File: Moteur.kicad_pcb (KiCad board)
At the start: 2 copper layers, 0 parts

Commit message: Couche PCB Définie
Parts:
- added C10: 10n, _0603, F.Cu at (76.2, 72.4)
- added C11, C12: 10pF, _0603, F.Cu at (0.00, 0.00)
- added C13, C6, C7, C9: 100n, _0603, F.Cu at (0.00, 0.00)
- added C14, C16: 47nF, SM1206, F.Cu at (0.00, 0.00)
- added C15: 47nF, SM1206, F.Cu at (48.3, 69.8)
- added R11: 100k, SM0805, F.Cu at (59.7, 52.1)
- added R8: 100k, SM0805, F.Cu at (34.3, 29.2)
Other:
- copper layers 2 -> 4
- net class Default: clearance 0.254 -> 0.204; trace_width 0.254 -> 0.204; via_dia 0.889 -> 0.8; via_drill 0.635 -> 0.3
- rule trace_clearance: 0.254 -> 0.204
- rule trace_min: 0.254 -> 0.204
- rule via_min_drill: 0.508 -> 0.3
- rule via_min_size: 0.889 -> 0.8

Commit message: footprints
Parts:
- added C1, C5: 100n, _0603, F.Cu at (0.00, 0.00)
- added C17, C8: 1uF, _0603, F.Cu at (0.00, 0.00)
- added C18: C, _0603, F.Cu at (0.00, 0.00)
- added C2: 100nF, _0603, F.Cu at (0.00, 0.00)
- added C3: 4.7uF, _0603, F.Cu at (0.00, 0.00)
- added C4: 470n, _0603, F.Cu at (0.00, 0.00)
- added D1: DIODESCH, CVRA-SOD80C, F.Cu at (0.00, 0.00)
- added D2: DEL_RGB, LedRGB, F.Cu at (0.00, 0.00)
- added IC1: TPS71501, CVRA-SOT23-5, F.Cu at (0.00, 0.00)
- added IC3: MAX3051, _SOT23-8, F.Cu at (0.00, 0.00)
- added JP1: JUMPER, Jumer, F.Cu at (0.00, 0.00)
- added L1: INDUCTOR, _0603, F.Cu at (0.00, 0.00)
- added P1: Bus2, _Pin2mm_4z, F.Cu at (0.00, 0.00)
- added P2: MotorEnc, _Pin2mm_5z, F.Cu at (0.00, 0.00)
- added P3: Bus1, _Pin2mm_4z, F.Cu at (0.00, 0.00)
- added P4: Motor, _Pin2mm_2, F.Cu at (0.00, 0.00)
- added P5: DBG, _Pin2mm_7z, F.Cu at (0.00, 0.00)
- added P6: PWR, _Pin2mm_2, F.Cu at (0.00, 0.00)
- added P7: GPIO, _Pin2mm_5z, F.Cu at (0.00, 0.00)
- added R1: 5.6M, _0603, F.Cu at (0.00, 0.00)
- added R10: 0.01R, CVRA-1206-1, F.Cu at (0.00, 0.00)
- added R12, R13: R, _0603, F.Cu at (0.00, 0.00)
- added R2: 910k, _0603, F.Cu at (0.00, 0.00)
- added R3: 0R, _0603, F.Cu at (0.00, 0.00)
- added R4: 22, _0603, F.Cu at (0.00, 0.00)
- added R5: 47, _0603, F.Cu at (0.00, 0.00)
- added R6: 39, _0603, F.Cu at (0.00, 0.00)
- added R7: 120, _0603, F.Cu at (0.00, 0.00)
- added R9: 330, _0603, F.Cu at (0.00, 0.00)
- added U1: STM32F303CCT6, _LQFP48, F.Cu at (0.00, 0.00)
- added X1: 16MHz, _TSX-3225-SMD-XTAL, F.Cu at (0.00, 0.00)
- C14, C16: footprint SM1206 -> _0603
- C15: value 47nF -> 100nF; footprint SM1206 -> _0603
- R11, R8: footprint SM0805 -> _0603
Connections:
- C10 pad 1: N-000002 -> +3.3V_A

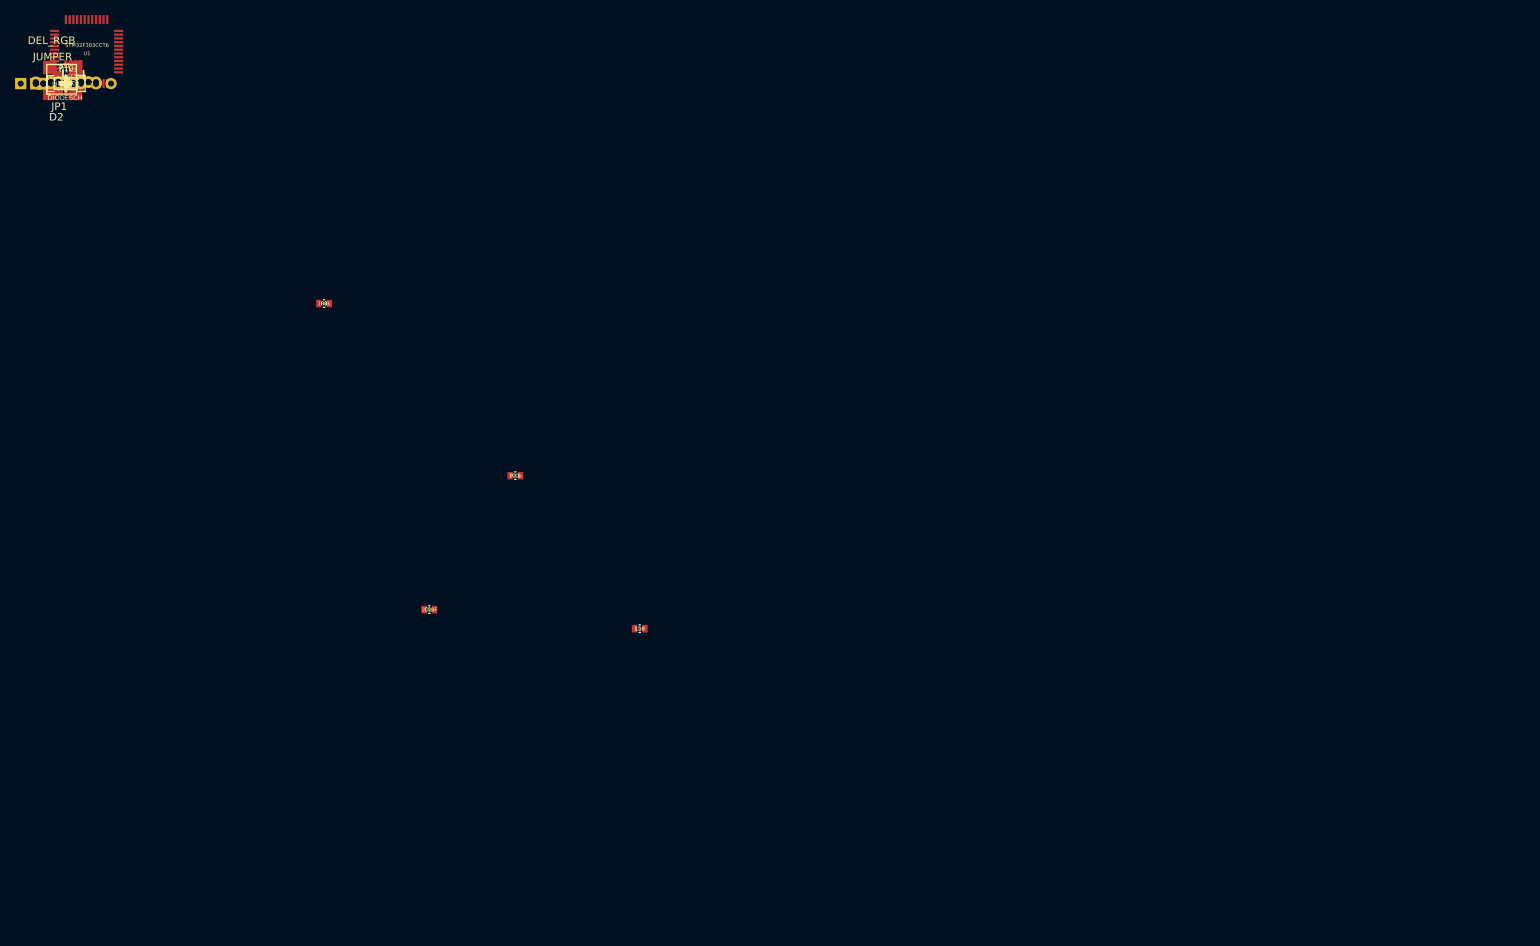
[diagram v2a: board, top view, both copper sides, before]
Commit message: Update footprint link, disperse component on PCB and add pcb size
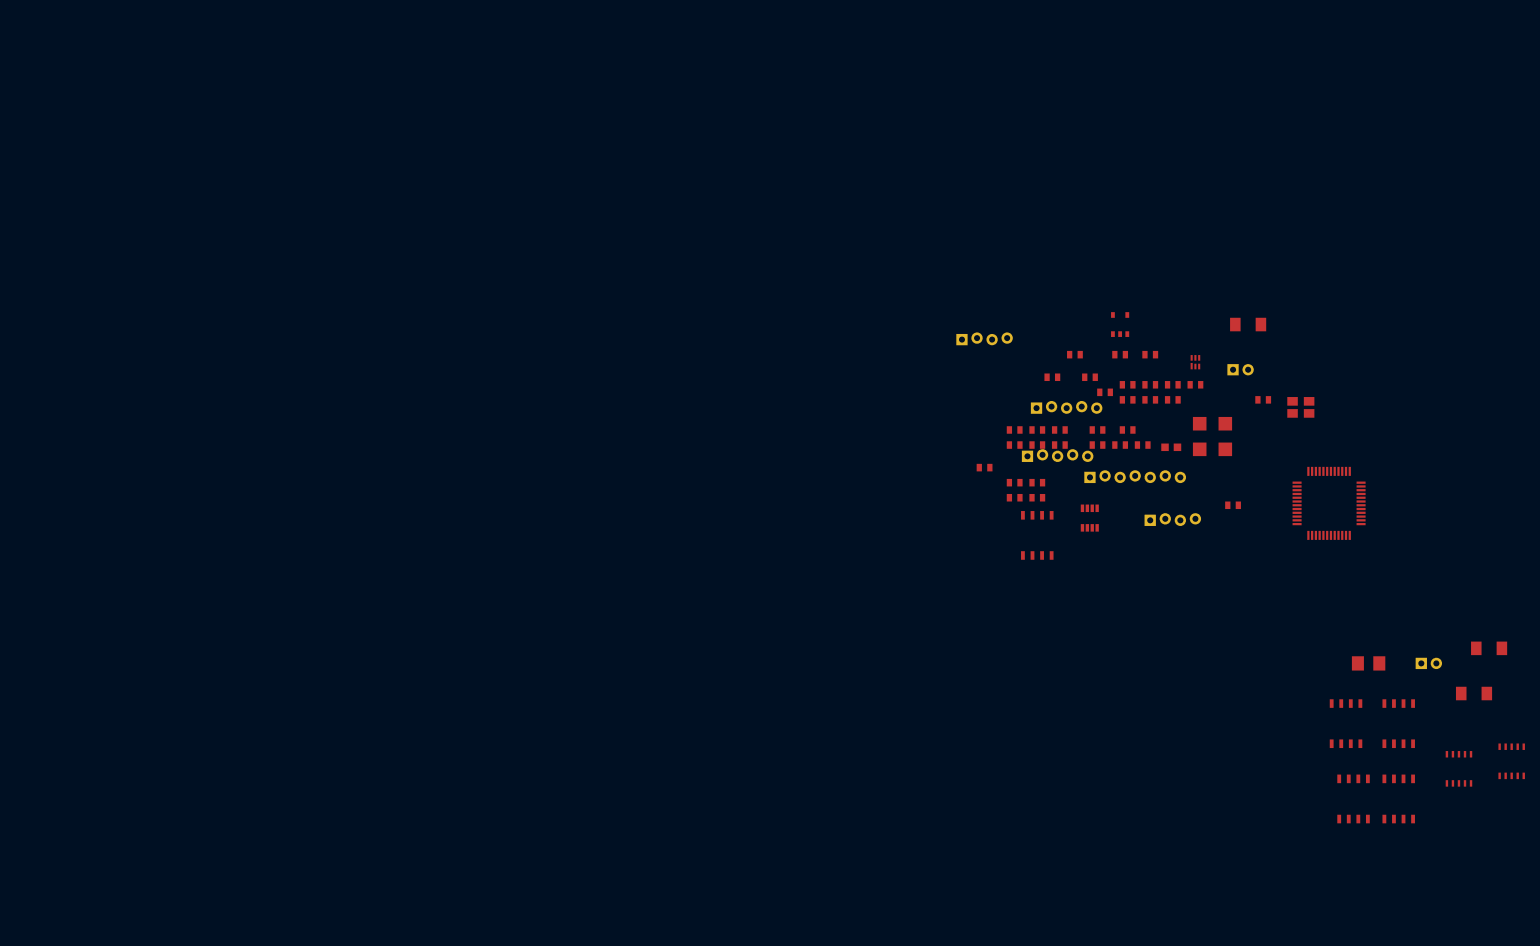
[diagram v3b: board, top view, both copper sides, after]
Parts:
- added D3: BAV102, CVRA-SOD80C, F.Cu at (189.0, 75.0)
- added D4: BAV102, CVRA-SOD80C, F.Cu at (187.0, 81.0)
- added IC2: TLV710, CVRA-PWSON-N6, F.Cu at (150.0, 37.0)
- added IC4: LM5106, PSONL10, F.Cu at (185.0, 91.0)
- added IC5: LM5106, PSONL10, F.Cu at (192.0, 90.0)
- added IC6: INA282, CVRA-SO8E, F.Cu at (129.0, 60.0)
- added Q1: IRF8721, CVRA-SO8E, F.Cu at (177.0, 85.0)
- added Q2: IRF8721, CVRA-SO8E, F.Cu at (171.0, 95.0)
- added Q3: IRF8721, CVRA-SO8E, F.Cu at (177.0, 95.0)
- added Q4: IRF8721, CVRA-SO8E, F.Cu at (170.0, 85.0)
- moved P4 196.7 mm to (181.0, 77.0)
- moved R10 189.4 mm to (173.0, 77.0)
- moved U1 175.6 mm to (165.0, 60.0)
- moved X1 169.5 mm to (164.0, 43.0)
- moved P6 160.6 mm to (156.0, 38.0)
- moved D1 160.2 mm to (157.0, 32.0)
- moved D2 159.9 mm to (152.7, 47.3)
- moved P1 158.0 mm to (147.0, 58.0)
- moved R6 155.2 mm to (150.0, 40.0)
- moved JP1 154.4 mm to (146.6, 48.3)
- moved C8 152.9 mm to (147.0, 42.0)
- moved C17 152.3 mm to (147.0, 40.0)
- moved P5 151.3 mm to (142.0, 52.3)
- moved C7 150.8 mm to (143.0, 48.0)
- moved C16 150.0 mm to (144.0, 42.0)
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
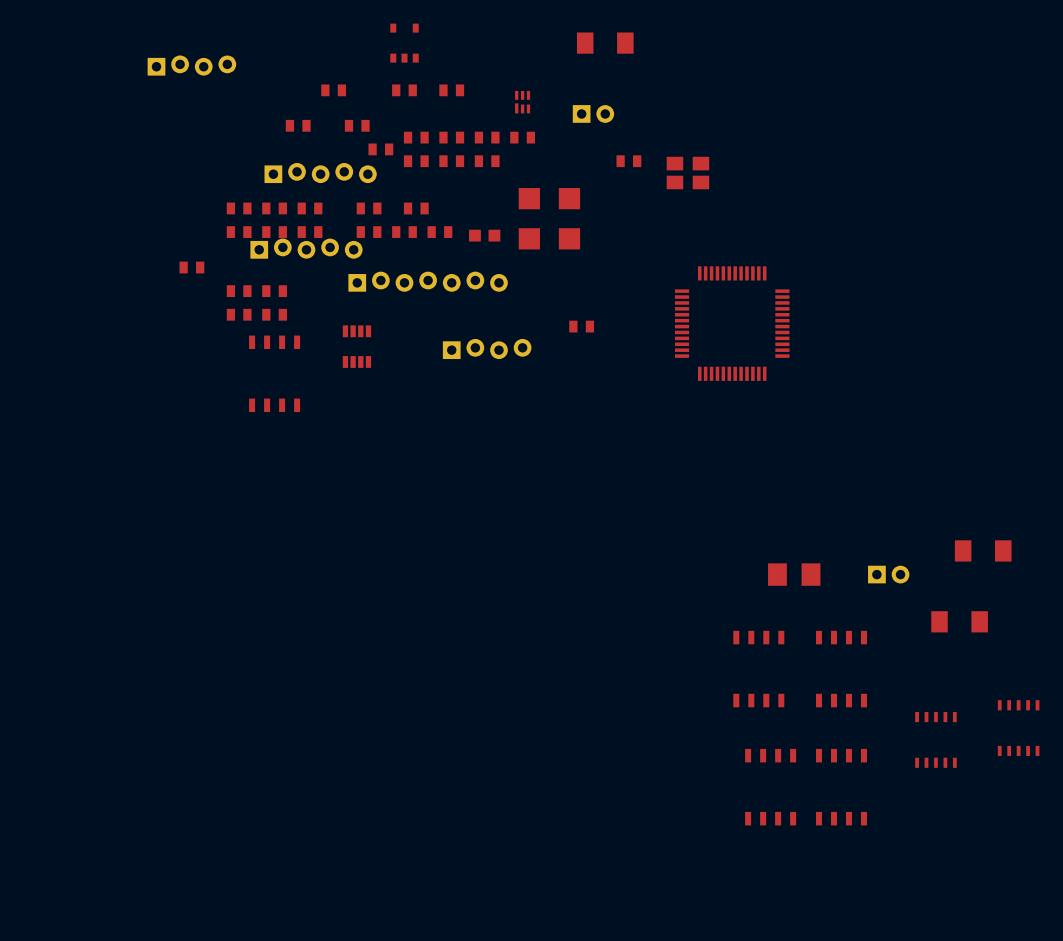
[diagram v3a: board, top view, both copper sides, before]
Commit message: Add board outline and placed power stage
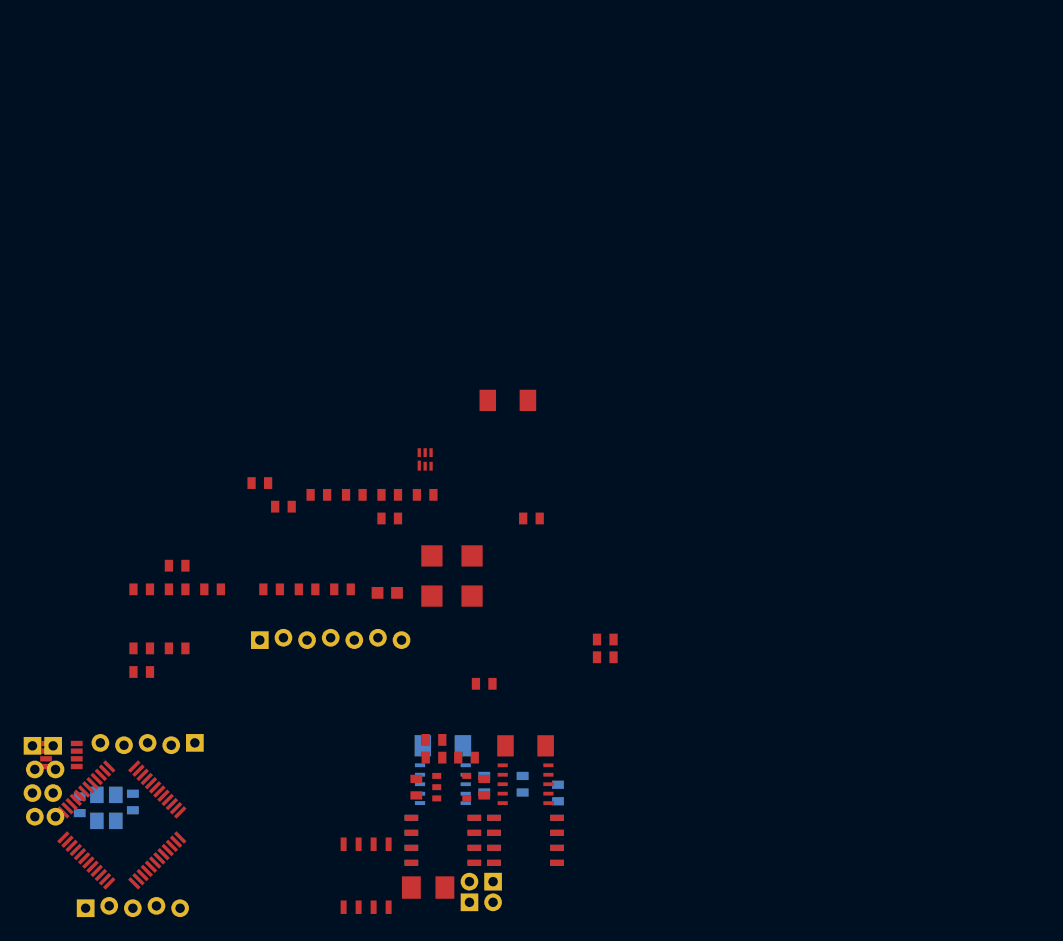
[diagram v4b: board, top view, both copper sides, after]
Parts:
- C11, C12, C14, C16, D4, IC5, Q3, Q4, R8, X1: moved to B.Cu
- moved X1 72.9 mm to (114.8, 96.8), turned to 90 degrees
- moved P6 65.7 mm to (146.5, 103.0), turned to 180 degrees
- moved C11 64.5 mm to (117.0, 96.2), turned to 270 degrees
- moved IC1 63.1 mm to (144.0, 95.0), turned to 270 degrees
- moved P3 62.0 mm to (108.5, 94.5), turned to 270 degrees
- moved R8 60.6 mm to (153.0, 95.5), turned to 90 degrees
- moved U1 60.0 mm to (115.0, 93.2), turned to 225 degrees
- moved R11 59.4 mm to (141.0, 95.0), turned to 90 degrees
- moved P2 57.7 mm to (117.0, 105.2)
- moved C16 52.8 mm to (146.8, 94.8), turned to 270 degrees
- moved P1 51.8 mm to (110.2, 94.5), turned to 270 degrees
- moved R2 50.5 mm to (142.5, 92.5)
- moved P7 50.3 mm to (118.2, 91.2), turned to 180 degrees
- moved C18 49.7 mm to (157.0, 84.0)
- moved C14 49.6 mm to (150.0, 94.8), turned to 270 degrees
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
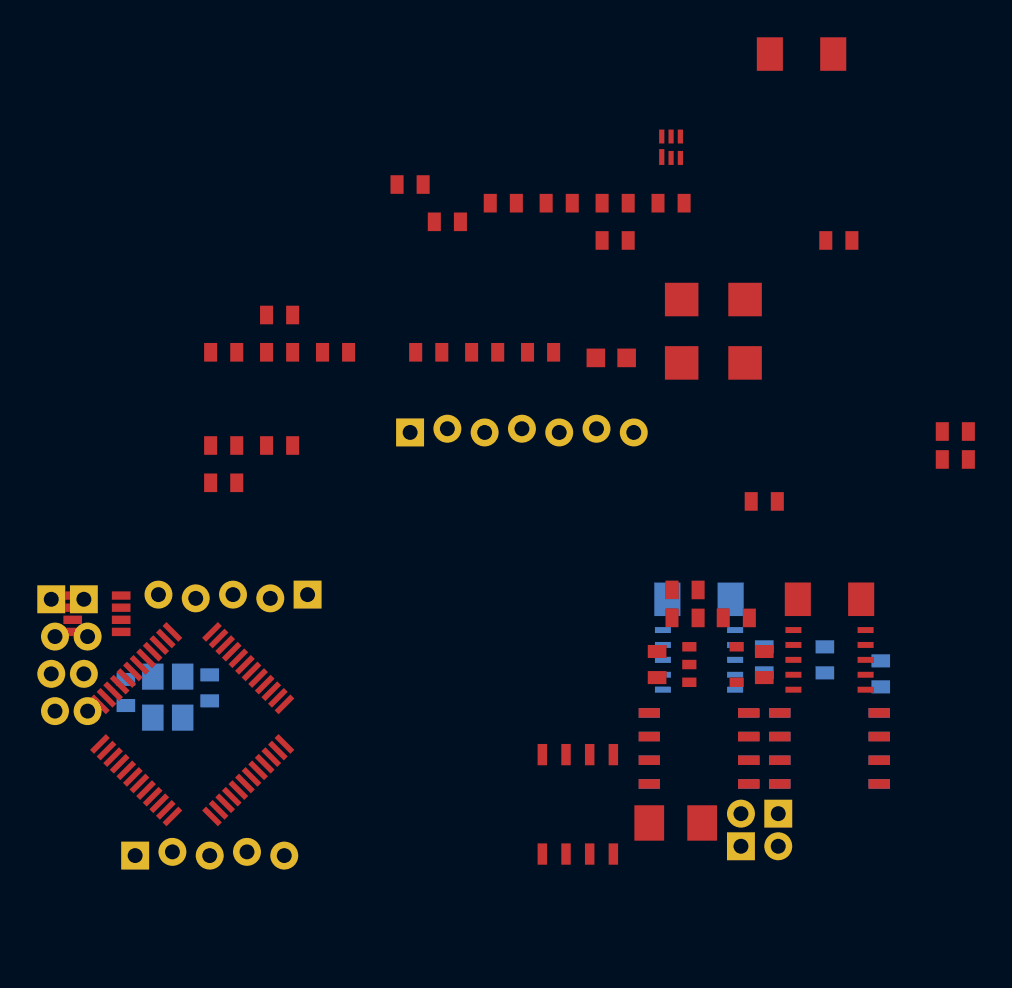
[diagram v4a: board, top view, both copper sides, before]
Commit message: Placement driver can
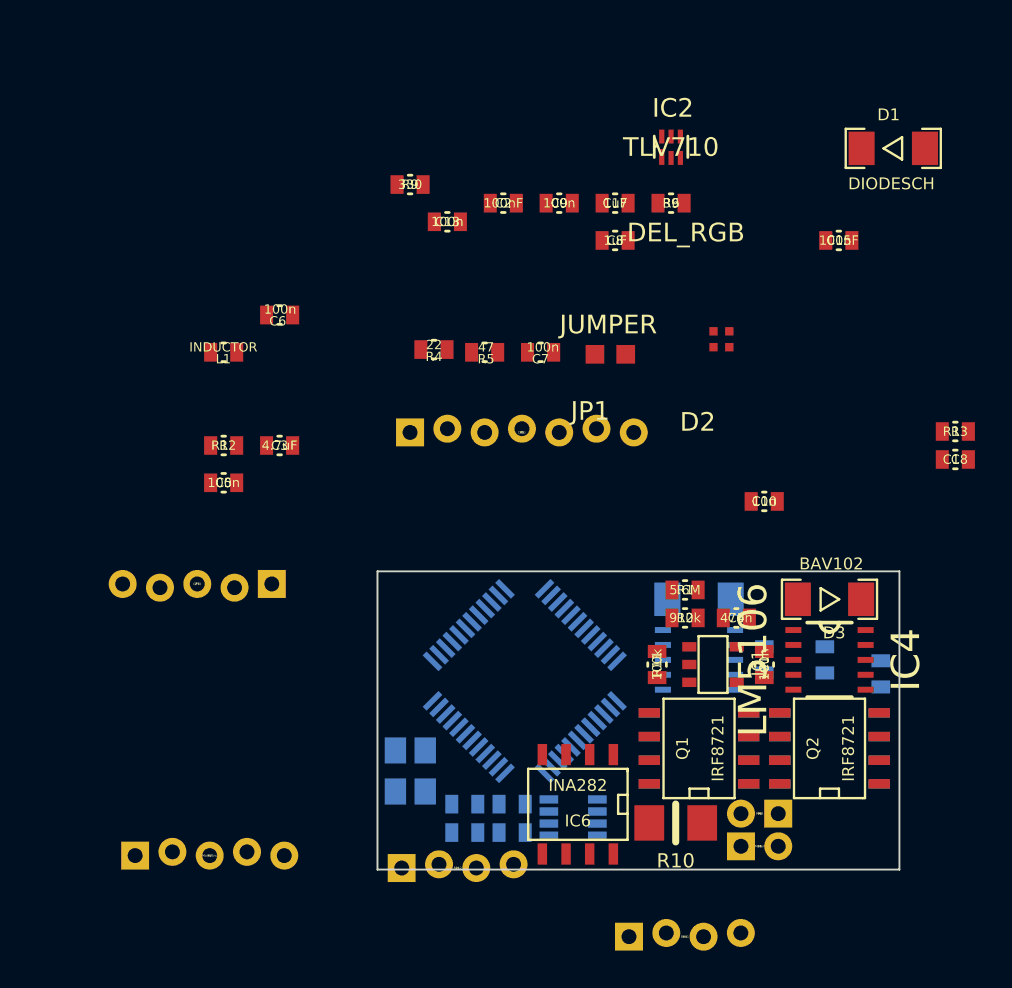
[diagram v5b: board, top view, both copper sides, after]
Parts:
- D2: footprint LedRGB -> Led_RGB
- IC3, R3, R7, U1: moved to B.Cu
- moved P3 37.2 mm to (142.5, 109.6), turned to 0 degrees
- moved R7 28.6 mm to (133.2, 104.0)
- moved IC3 27.1 mm to (137.8, 102.2), turned to 270 degrees
- moved R3 26.0 mm to (133.2, 102.5)
- moved P1 23.1 mm to (130.3, 105.9), turned to 0 degrees
- moved U1 19.4 mm to (132.8, 100.8), turned to 135 degrees
- moved C12 19.1 mm to (130.7, 102.5), turned to 180 degrees
- moved C11 15.7 mm to (130.7, 104.0), turned to 0 degrees
- moved X1 13.6 mm to (127.8, 100.7), turned to 270 degrees
- moved D1 7.06 mm to (153.7, 67.3)
- moved P7 2.00 mm to (116.3, 90.7)
- moved R4 0.32 mm to (129.0, 78.1)
- moved JP1 0.20 mm to (138.3, 78.4)
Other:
- board outline added: 28 x 16 mm

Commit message: final schematic review, component placement
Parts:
- removed JP1: JUMPER, Jumer
- removed P7: GPIO, _Pin2mm_5z
- removed R7: 120, _0603
- C10, C13, C15, C2, C3, C6, C7, C8, C9, IC2, IC6, P5, R10, R9: moved to B.Cu
- C11, C12, C14, R8, U1, X1: moved to F.Cu
- D2: value DEL_RGB -> LED; footprint Led_RGB -> _0603
- P1: footprint _Pin2mm_4z -> pin4_can_connector
- P2: value MotorEnc -> CONN_6; footprint _Pin2mm_5z -> _Pin2mm_6z
- P3: value Bus1 -> GPIO; footprint _Pin2mm_4z -> _Pin2mm_6z
- P4: value Motor -> CONN_1
- P6: value PWR -> CONN_1
- R3: value 0R -> 10k
- R5: value 47 -> 10k
- R6: value 39 -> 10k
- moved D1 38.9 mm to (124.2, 92.7), turned to 270 degrees
- moved P2 37.2 mm to (153.4, 97.8), turned to 90 degrees
- moved R4 36.0 mm to (163.3, 89.2)
- moved C18 35.4 mm to (135.4, 112.0)
- moved R13 35.2 mm to (135.4, 110.2)
- moved C17 35.0 mm to (161.5, 96.8), turned to 270 degrees
- moved R11 32.2 mm to (173.2, 94.7), turned to 180 degrees
- moved IC2 31.7 mm to (124.7, 94.0)
- moved R12 30.9 mm to (132.8, 110.2)
- moved C13 30.9 mm to (130.8, 102.1), turned to 270 degrees
- moved R9 30.4 mm to (137.4, 98.0)
- moved C15 27.7 mm to (137.4, 96.5)
- moved C8 27.0 mm to (128.5, 97.3), turned to 180 degrees
- moved C9 26.6 mm to (133.3, 96.8)
- moved C6 25.4 mm to (133.3, 98.3)
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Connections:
- C15 pad 1: ADC/I_BAT -> ADC/I_MOT
- C5 pad 1: N-0000022 -> Reset
- IC3 pad 8: N-0000013 -> CAN_SPEED
- P2 pad 1: I -> Mot-
- P2 pad 2: B -> Mot+
- P2 pad 3: A -> GND
- P2 pad 4: GND -> +5V_protected
- P2 pad 5: +5V_protected -> B
- P3 pad 1: CANL -> GPIO_ADC
- P3 pad 2: CANH -> I
- P3 pad 3: GND -> GPIO_B
- P3 pad 4: +5V -> GPIO_A
- P4 pad 1: Mot- -> +BATT
- P4 pad 2: Mot+ -> (no net)
- P5 pad 3: (no net) -> Swdclk
- P5 pad 4: (no net) -> Swdio
- P5 pad 5: (no net) -> Reset
- P6 pad 2: +BATT -> (no net)
- R3 pad 1: N-0000012 -> +5V_protected
- R3 pad 2: N-0000013 -> GPIO_A
- R4 pad 1: N-0000068 -> LED
- R5 pad 1: N-0000069 -> +5V_protected
- R5 pad 2: N-0000067 -> GPIO_B
- R6 pad 1: LEDR -> +5V_protected
- R6 pad 2: N-0000046 -> I
- R9 pad 1: ADC/I_BAT -> ADC/I_MOT
- U1 pad 10: (no net) -> GPIO_ADC
- U1 pad 11: (no net) -> LED
- U1 pad 12: LEDR -> (no net)
- U1 pad 13: N-0000068 -> (no net)
- U1 pad 14: ADC/V_BAT -> CAN_SPEED
- U1 pad 15: (no net) -> ADC/I_MOT
- U1 pad 16: (no net) -> ADC/V_BAT
- U1 pad 19: I -> (no net)
- U1 pad 20: N-0000012 -> (no net)
- U1 pad 33: N-0000069 -> I
- U1 pad 34: (no net) -> Swdio
- U1 pad 37: (no net) -> Swdclk
- U1 pad 7: N-0000022 -> Reset
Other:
- board size 28 x 16 mm -> 31.8 x 16 mm
- board text added: "led on F.CU"

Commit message: placement
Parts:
- C18, R13: moved to B.Cu
- moved R6 15.5 mm to (138.2, 85.3)
- moved R11 14.5 mm to (160.3, 101.3)
- moved L1 11.2 mm to (126.2, 85.6)
- moved C18 10.9 mm to (134.6, 101.1)
- moved R12 8.49 mm to (139.4, 104.9), turned to 180 degrees
- moved R13 7.66 mm to (134.6, 102.6)
- moved R5 6.61 mm to (132.3, 84.8)
- moved C1 2.34 mm to (143.5, 105.7), turned to 180 degrees
- moved IC6 0.76 mm to (139.4, 102.4), turned to 180 degrees
- moved P3 0.51 mm to (130.0, 104.9)
- moved P1 0.51 mm to (123.4, 99.8)
